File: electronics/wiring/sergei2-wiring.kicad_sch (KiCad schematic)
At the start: 27 parts, among them J1 6i25 port 1, J2 6i25 port 2, M1 UGRMEM, M2 UGRMEM, M3 MY1016, SW1 ESTOP, SW2 Mode switch, SW4 Door closed, U1 Power_control_PCB

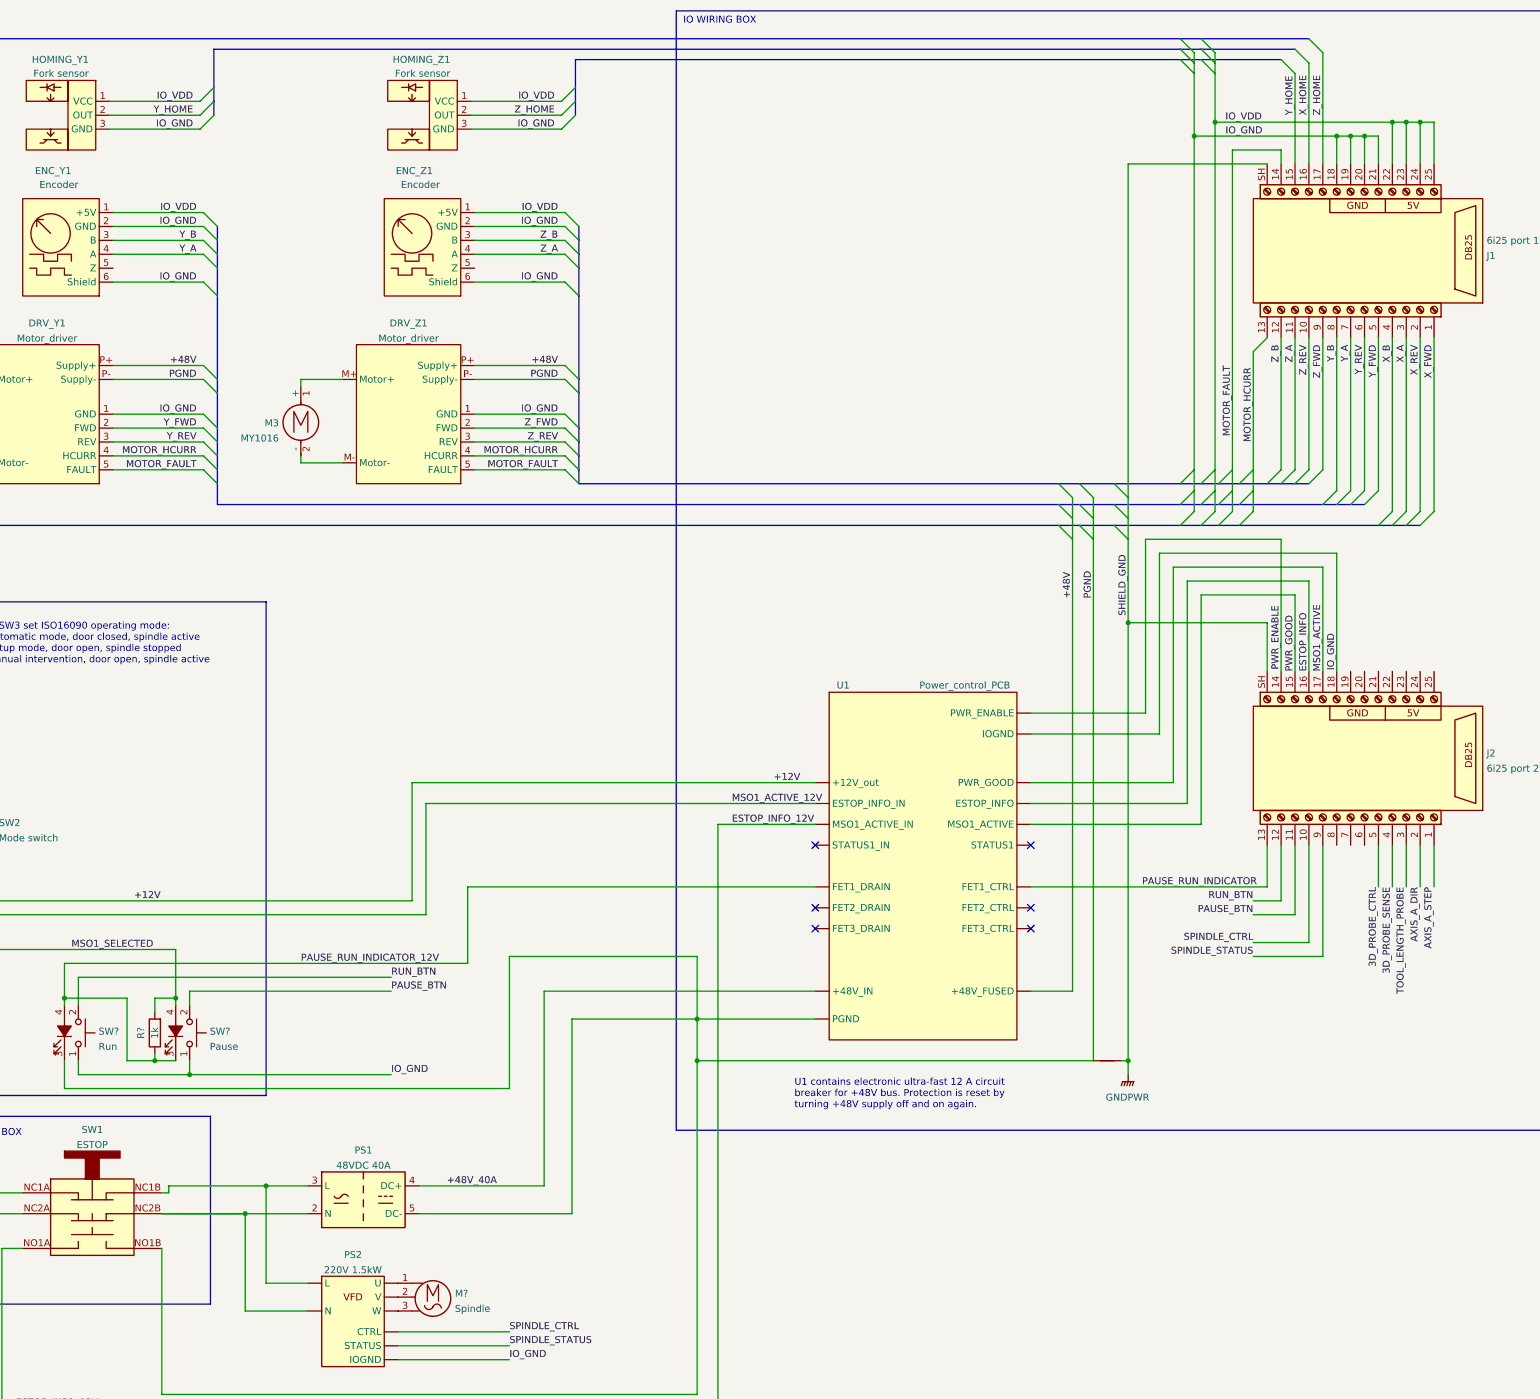
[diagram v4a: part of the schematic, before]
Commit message: Add homing config
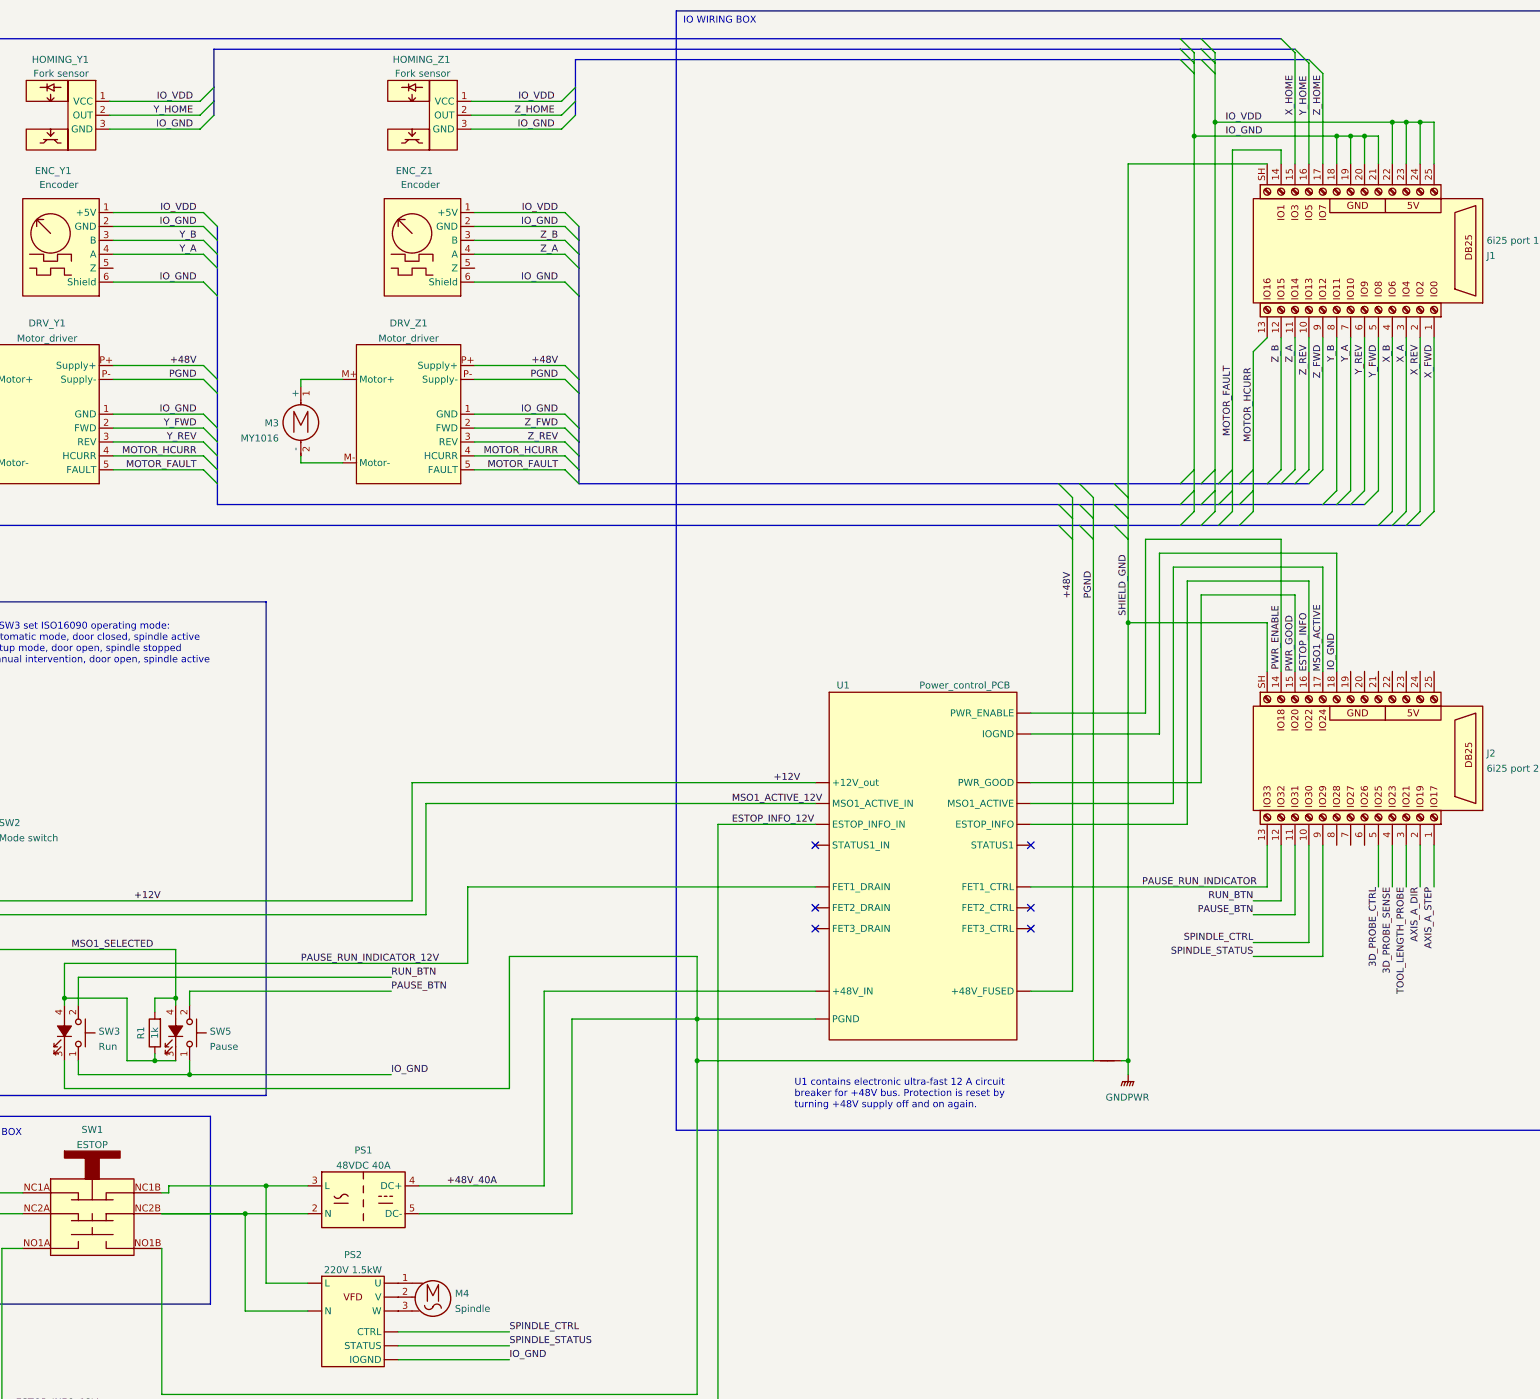
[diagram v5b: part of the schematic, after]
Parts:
- J2: symbol sergei2_wiring:DB25_breakout -> sergei2_wiring:DB25_breakout_1
- gave numbers to parts that had none: 5
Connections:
- net X_HOME: now also J1.15; no longer J1.16
- net Y_HOME: now also J1.16; no longer J1.15
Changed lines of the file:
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@@
     (stroke (width 0) (type default) (color 0 0 0 0))
+  )
+  (bus_entry (at 339.09 22.86) (size 2.54 2.54)
+    (stroke (width 0.4) (type default) (color 194 194 194 1))
   )
   (bus_entry (at 210.185 36.83) (size -2.54 2.54)
@@
     (stroke (width 0) (type default) (color 0 0 0 0))
   )
-  (bus_entry (at 339.09 26.67) (size 2.54 2.54)
-    (stroke (width 0.4) (type default) (color 194 194 194 1))
-  )
-  (bus_entry (at 344.17 22.86) (size 2.54 2.54)
-    (stroke (width 0.4) (type default) (color 194 194 194 1))
-  )
   (bus_entry (at 341.63 24.765) (size 2.54 2.54)
     (stroke (width 0.4) (type default) (color 194 194 194 1))
@@
     (stroke (width 0) (type default) (color 0 0 0 0))
   )
+  (bus_entry (at 344.17 26.67) (size 2.54 2.54)
+    (stroke (width 0.4) (type default) (color 194 194 194 1))
+  )
   (bus_entry (at 142.24 85.09) (size 2.54 2.54)
     (stroke (width 0) (type default) (color 0 0 0 0))
@@
     (stroke (width 0) (type default) (color 0 0 0 0))
   )
-  (wire (pts (xy 321.945 162.56) (xy 321.945 121.92))
-    (stroke (width 0) (type default) (color 0 0 0 0))
-  )
-  (wire (pts (xy 293.37 162.56) (xy 321.945 162.56))
-    (stroke (width 0) (type default) (color 0 0 0 0))
-  )
   (wire (pts (xy 74.93 91.44) (xy 58.42 91.44))
     (stroke (width 0) (type default) (color 0 0 0 0))
@@
     (stroke (width 0) (type default) (color 0 0 0 0))
   )
+  (wire (pts (xy 293.37 158.75) (xy 324.485 158.75))
+    (stroke (width 0) (type default) (color 0 0 0 0))
+  )
   (wire (pts (xy 208.28 96.52) (xy 191.77 96.52))
     (stroke (width 0) (type default) (color 0 0 0 0))
@@
     (stroke (width 0) (type default) (color 0 0 0 0))
   )
-  (wire (pts (xy 293.37 158.75) (xy 319.405 158.75))
-    (stroke (width 0) (type default) (color 0 0 0 0))
-  )
-  (wire (pts (xy 319.405 158.75) (xy 319.405 119.38))
+  (wire (pts (xy 319.405 119.38) (xy 319.405 162.56))
     (stroke (width 0) (type default) (color 0 0 0 0))
   )
@@
     (stroke (width 0) (type default) (color 132 132 132 1))
   )
-  (bus (pts (xy 324.485 22.86) (xy 344.17 22.86))
+  (bus (pts (xy 324.485 22.86) (xy 339.09 22.86))
     (stroke (width 0) (type default) (color 132 132 132 1))
   )
@@
     (stroke (width 0) (type default) (color 0 0 0 0))
   )
+  (wire (pts (xy 319.405 162.56) (xy 293.37 162.56))
+    (stroke (width 0) (type default) (color 0 0 0 0))
+  )
   (wire (pts (xy 149.86 237.49) (xy 161.29 237.49))
     (stroke (width 0.7) (type default) (color 0 0 255 1))
@@
     (stroke (width 0.4) (type default) (color 0 0 132 1))
   )
-  (wire (pts (xy 346.71 45.72) (xy 346.71 25.4))
+  (wire (pts (xy 346.71 45.72) (xy 346.71 29.21))
     (stroke (width 0.4) (type default) (color 194 194 194 1))
   )
@@
     (stroke (width 0) (type default) (color 0 0 0 0))
   )
+  (wire (pts (xy 321.945 121.92) (xy 321.945 166.37))
+    (stroke (width 0) (type default) (color 0 0 0 0))
+  )
   (wire (pts (xy 311.15 110.49) (xy 311.15 114.3))
     (stroke (width 0) (type default) (color 0 0 0 0))
@@
     (stroke (width 0) (type default) (color 0 0 0 0))
   )
+  (wire (pts (xy 321.945 166.37) (xy 293.37 166.37))
+    (stroke (width 0) (type default) (color 0 0 0 0))
+  )
   (wire (pts (xy 208.28 99.06) (xy 191.77 99.06))
     (stroke (width 0) (type default) (color 0 0 0 0))
@@
     (stroke (width 0) (type default) (color 0 0 0 0))
   )
-  (wire (pts (xy 341.63 45.72) (xy 341.63 29.21))
+  (wire (pts (xy 341.63 45.72) (xy 341.63 25.4))
     (stroke (width 0.4) (type default) (color 194 194 194 1))
   )
@@
     (stroke (width 0) (type default) (color 0 0 0 0))
   )
-  (wire (pts (xy 324.485 166.37) (xy 324.485 124.46))
-    (stroke (width 0) (type default) (color 0 0 0 0))
-  )
-  (wire (pts (xy 293.37 166.37) (xy 324.485 166.37))
+  (wire (pts (xy 324.485 124.46) (xy 324.485 158.75))
     (stroke (width 0) (type default) (color 0 0 0 0))
   )
@@
     (stroke (width 0) (type default) (color 0 0 0 0))
   )
-  (bus (pts (xy 324.485 26.67) (xy 339.09 26.67))
+  (bus (pts (xy 324.485 26.67) (xy 344.17 26.67))
     (stroke (width 0) (type default) (color 132 132 132 1))
   )
@@
     (effects (font (size 1.27 1.27)) (justify right bottom))
   )
-  (label "X_HOME" (at 344.17 36.83 90)
+  (label "X_HOME" (at 341.63 36.83 90)
     (effects (font (size 1.27 1.27)) (justify left bottom))
   )
@@
     (effects (font (size 1.27 1.27)) (justify right bottom))
   )
-  (label "Y_HOME" (at 341.63 36.83 90)
+  (label "Y_HOME" (at 344.17 36.83 90)
     (effects (font (size 1.27 1.27)) (justify left bottom))
   )
@@
   (symbol (lib_id "Switch:SW_Push_LED") (at 116.84 204.47 270) (mirror x) (unit 1)
     (in_bom yes) (on_board yes) (fields_autoplaced)
-    (property "Reference" "SW?" (id 0) (at 123.063 204.1965 90)
+    (property "Reference" "SW3" (id 0) (at 123.063 204.1965 90)
       (effects (font (size 1.27 1.27)) (justify left))
     )
@@
   (symbol (lib_id "power:GNDPWR") (at 311.15 212.09 0) (unit 1)
     (in_bom yes) (on_board yes) (fields_autoplaced)
-    (property "Reference" "#PWR?" (id 0) (at 311.15 217.17 0)
+    (property "Reference" "#PWR01" (id 0) (at 311.15 217.17 0)
       (effects (font (size 1.27 1.27)) hide)
     )
@@
     (pin "1")
   )
-  (symbol (lib_id "sergei2_wiring:DB25_breakout") (at 351.79 154.94 270) (mirror x) (unit 1)
+  (symbol (lib_id "sergei2_wiring:DB25_breakout_1") (at 351.79 154.94 270) (mirror x) (unit 1)
     (in_bom yes) (on_board yes) (fields_autoplaced)
     (property "Reference" "J2" (id 0) (at 376.6312 153.3965 90)
@@
   (symbol (lib_id "Device:NetTie_2") (at 307.34 209.55 0) (unit 1)
     (in_bom yes) (on_board yes) (fields_autoplaced)
-    (property "Reference" "NT?" (id 0) (at 307.34 208.3585 0)
+    (property "Reference" "NT1" (id 0) (at 307.34 208.3585 0)
       (effects (font (size 1.27 1.27)) hide)
     )
@@
     (pin "1")
   )
-  (symbol (lib_id "sergei2_wiring:DB25_breakout") (at 351.79 62.23 270) (mirror x) (unit 1)
+  (symbol (lib_name "DB25_breakout_1") (lib_id "sergei2_wiring:DB25_breakout") (at 351.79 62.23 270) (mirror x) (unit 1)
     (in_bom yes) (on_board yes) (fields_autoplaced)
     (property "Reference" "J1" (id 0) (at 376.6312 62.5035 90)
@@
   (symbol (lib_id "sergei2_wiring:Motor_AC_3PHASE") (at 184.15 252.73 0) (unit 1)
     (in_bom yes) (on_board yes) (fields_autoplaced)
-    (property "Reference" "M?" (id 0) (at 188.1632 252.0755 0)
+    (property "Reference" "M4" (id 0) (at 188.1632 252.0755 0)
       (effects (font (size 1.27 1.27)) (justify left))
     )
@@
   (symbol (lib_id "Switch:SW_Push_LED") (at 137.16 204.47 270) (mirror x) (unit 1)
     (in_bom yes) (on_board yes) (fields_autoplaced)
-    (property "Reference" "SW?" (id 0) (at 143.383 204.1965 90)
+    (property "Reference" "SW5" (id 0) (at 143.383 204.1965 90)
       (effects (font (size 1.27 1.27)) (justify left))
     )
@@
   (symbol (lib_id "Device:R") (at 133.35 204.47 180) (unit 1)
     (in_bom yes) (on_board yes)
-    (property "Reference" "R?" (id 0) (at 130.81 204.47 90))
+    (property "Reference" "R1" (id 0) (at 130.81 204.47 90))
     (property "Value" "1k" (id 1) (at 133.35 204.47 90))
     (property "Footprint" "" (id 2) (at 135.128 204.47 90)
@@
   (symbol_instances
     (path "/0e070e4c-0ffd-4be8-b277-b40e096a342c"
-      (reference "#PWR?") (unit 1) (value "GNDPWR") (footprint "")
+      (reference "#PWR01") (unit 1) (value "GNDPWR") (footprint "")
     )
     (path "/db509c8b-17a5-4fb6-9854-eb3f85921c6a"
@@
     )
     (path "/da641bd4-a55a-44a1-9325-d69cc0139ea1"
-      (reference "M?") (unit 1) (value "Spindle") (footprint "")
+      (reference "M4") (unit 1) (value "Spindle") (footprint "")
     )
     (path "/7103568d-d58d-461a-b301-622a8570aa48"
-      (reference "NT?") (unit 1) (value "NetTie_2") (footprint "")
+      (reference "NT1") (unit 1) (value "NetTie_2") (footprint "")
     )
     (path "/72a4dc44-6488-443b-a406-8d698414ef4b"
@@
     )
     (path "/f7b9c560-0f67-4948-bca8-f21ca35f216c"
-      (reference "R?") (unit 1) (value "1k") (footprint "")
+      (reference "R1") (unit 1) (value "1k") (footprint "")
     )
     (path "/bb00da48-0bcb-467b-972e-34490eb05b08"
@@
       (reference "SW2") (unit 1) (value "Mode switch") (footprint "")
     )
+    (path "/0d9c3c96-694e-4526-b90f-7d8acb2d3db5"
+      (reference "SW3") (unit 1) (value "Run") (footprint "")
+    )
     (path "/f6f7d2e1-3f32-45c2-9fb9-bffdf35fa32e"
       (reference "SW4") (unit 1) (value "Door closed") (footprint "")
     )
-    (path "/0d9c3c96-694e-4526-b90f-7d8acb2d3db5"
-      (reference "SW?") (unit 1) (value "Run") (footprint "")
-    )
     (path "/e8b6fe3b-7384-49f6-9b8c-01ed77d809f0"
-      (reference "SW?") (unit 1) (value "Pause") (footprint "")
+      (reference "SW5") (unit 1) (value "Pause") (footprint "")
     )
     (path "/b9baa06b-85b7-4407-ae21-2078ad1192c1"
